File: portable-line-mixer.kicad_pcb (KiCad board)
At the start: 4 copper layers, 77.5 x 114.3 mm, 138 parts, among them J1 Power In (Male-top), J2 LCD Connection I2C, J3 Audio Out, J4 Audio IN, J5 Encoder Connection, SW1 Nano Reset, T1 PMV45EN2, U1 LM27762, U10 DS1882, U11 DS1882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

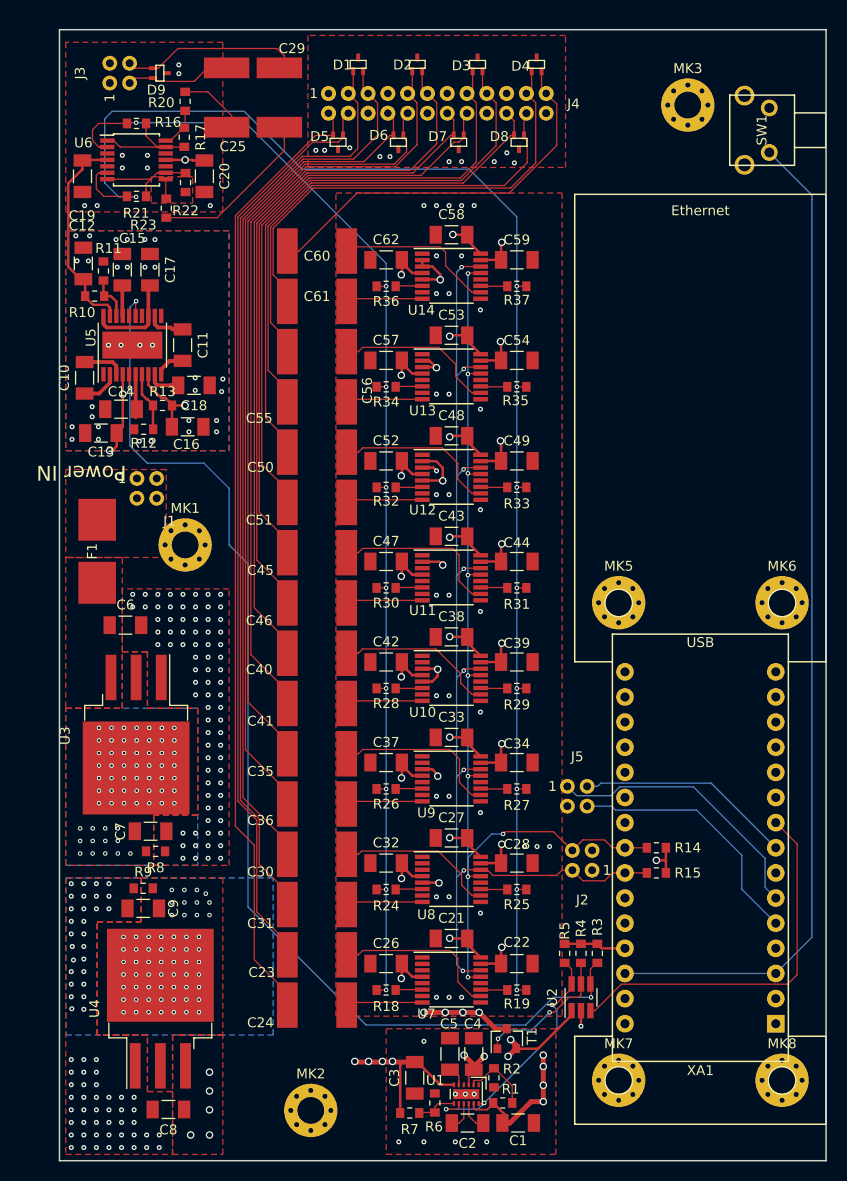
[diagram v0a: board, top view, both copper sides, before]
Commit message: Swapped right angle reset switch for straight
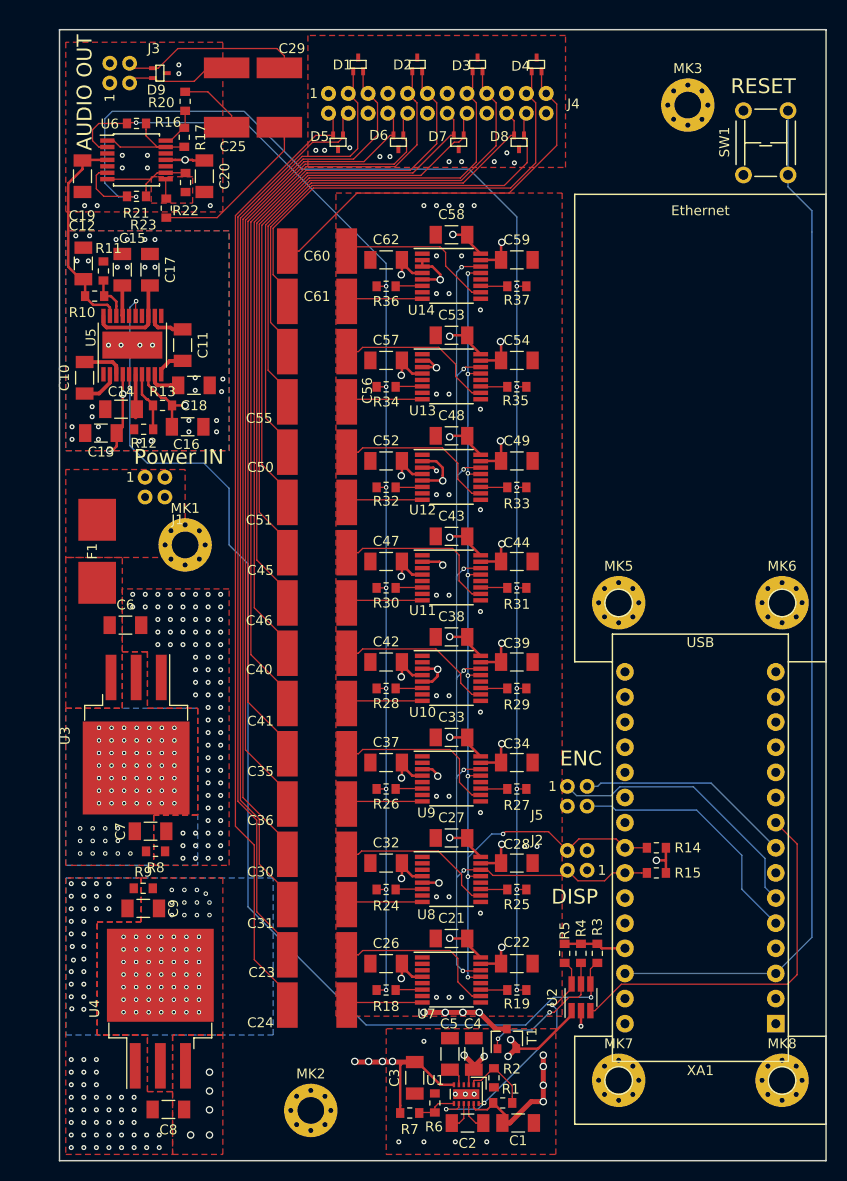
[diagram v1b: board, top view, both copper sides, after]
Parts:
- SW1: footprint SW-Eswitch:TL1105WF -> SW-Eswitch:TL1105
- moved SW1 1.55 mm to (136.8, 104.1), turned to 180 degrees
- moved J1 0.84 mm to (75.1, 138.9)
- moved J2 0.51 mm to (117.7, 176.7)
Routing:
- net /Arduino Nano Header Connections + Ethernet connection/Nano_RST: track 101.5 -> 105.0 mm
- net /Arduino Nano Header Connections + Ethernet connection/5V-SCL: track 111.4 -> 110.8 mm
- net GNDREF: track 3.52 -> 3.14 mm, vias 244 -> 243
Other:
- board text added: "AUDIO OUT"
- board text added: "DISP"
- board text added: "ENC"
- board text added: "RESET"
